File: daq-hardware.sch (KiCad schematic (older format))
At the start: 26 parts

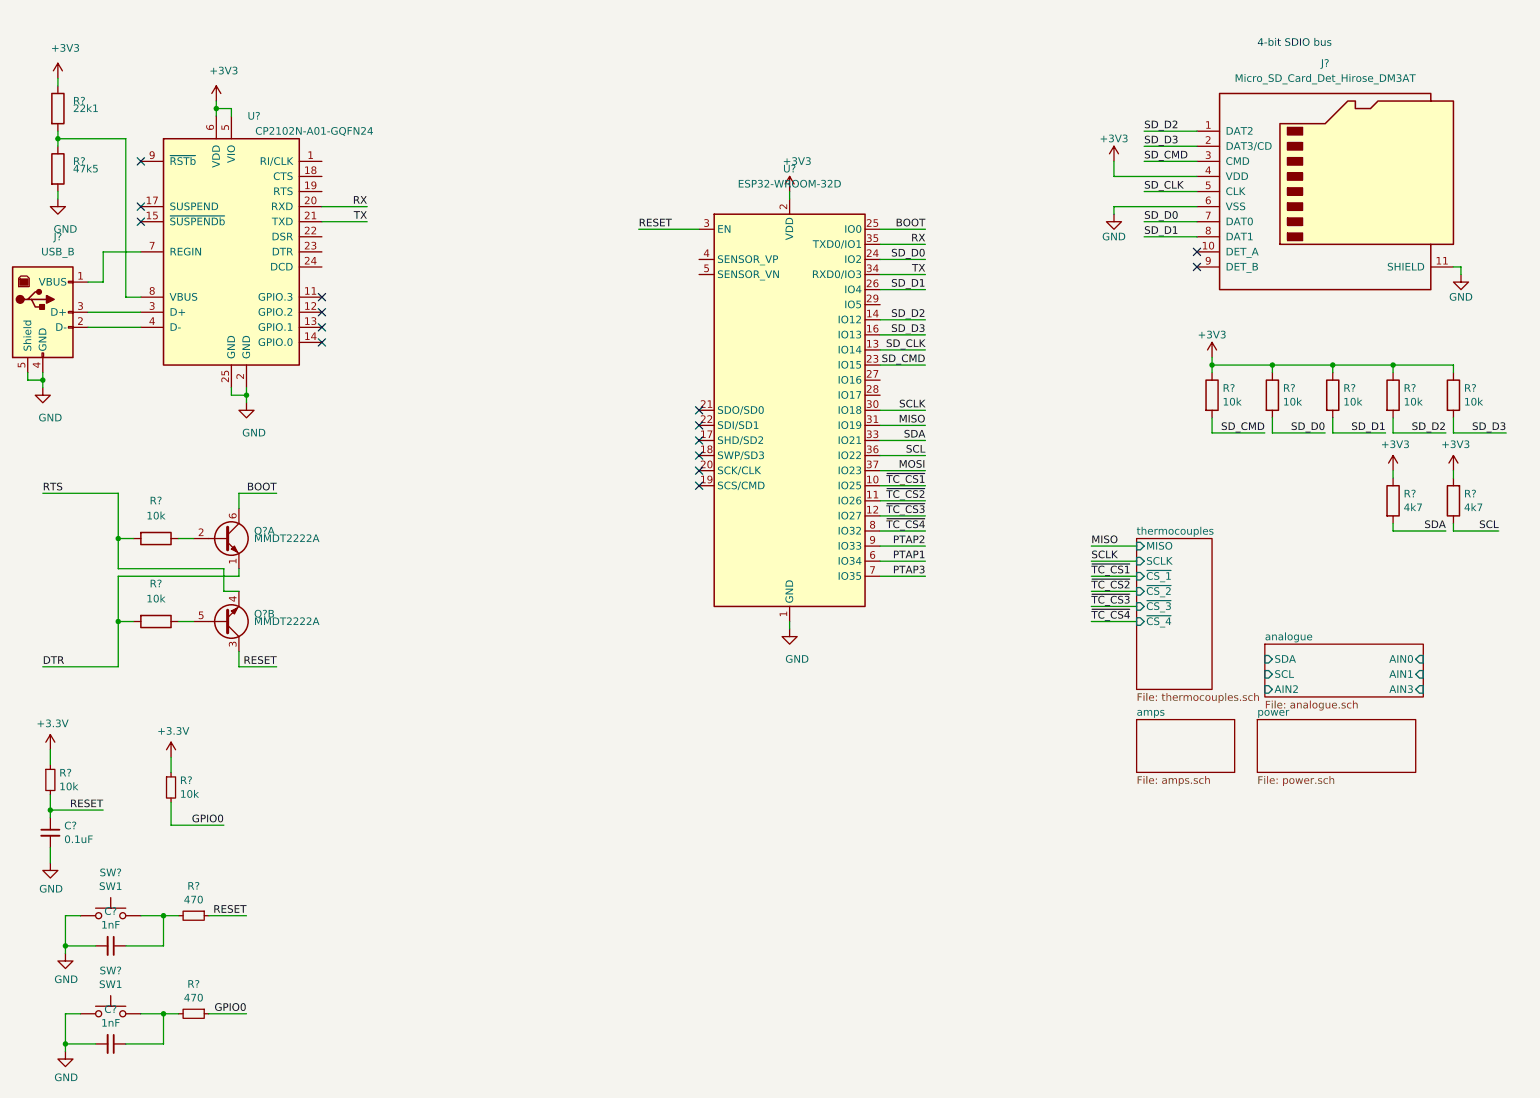
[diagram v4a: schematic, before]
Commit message: Added indicator LEDs
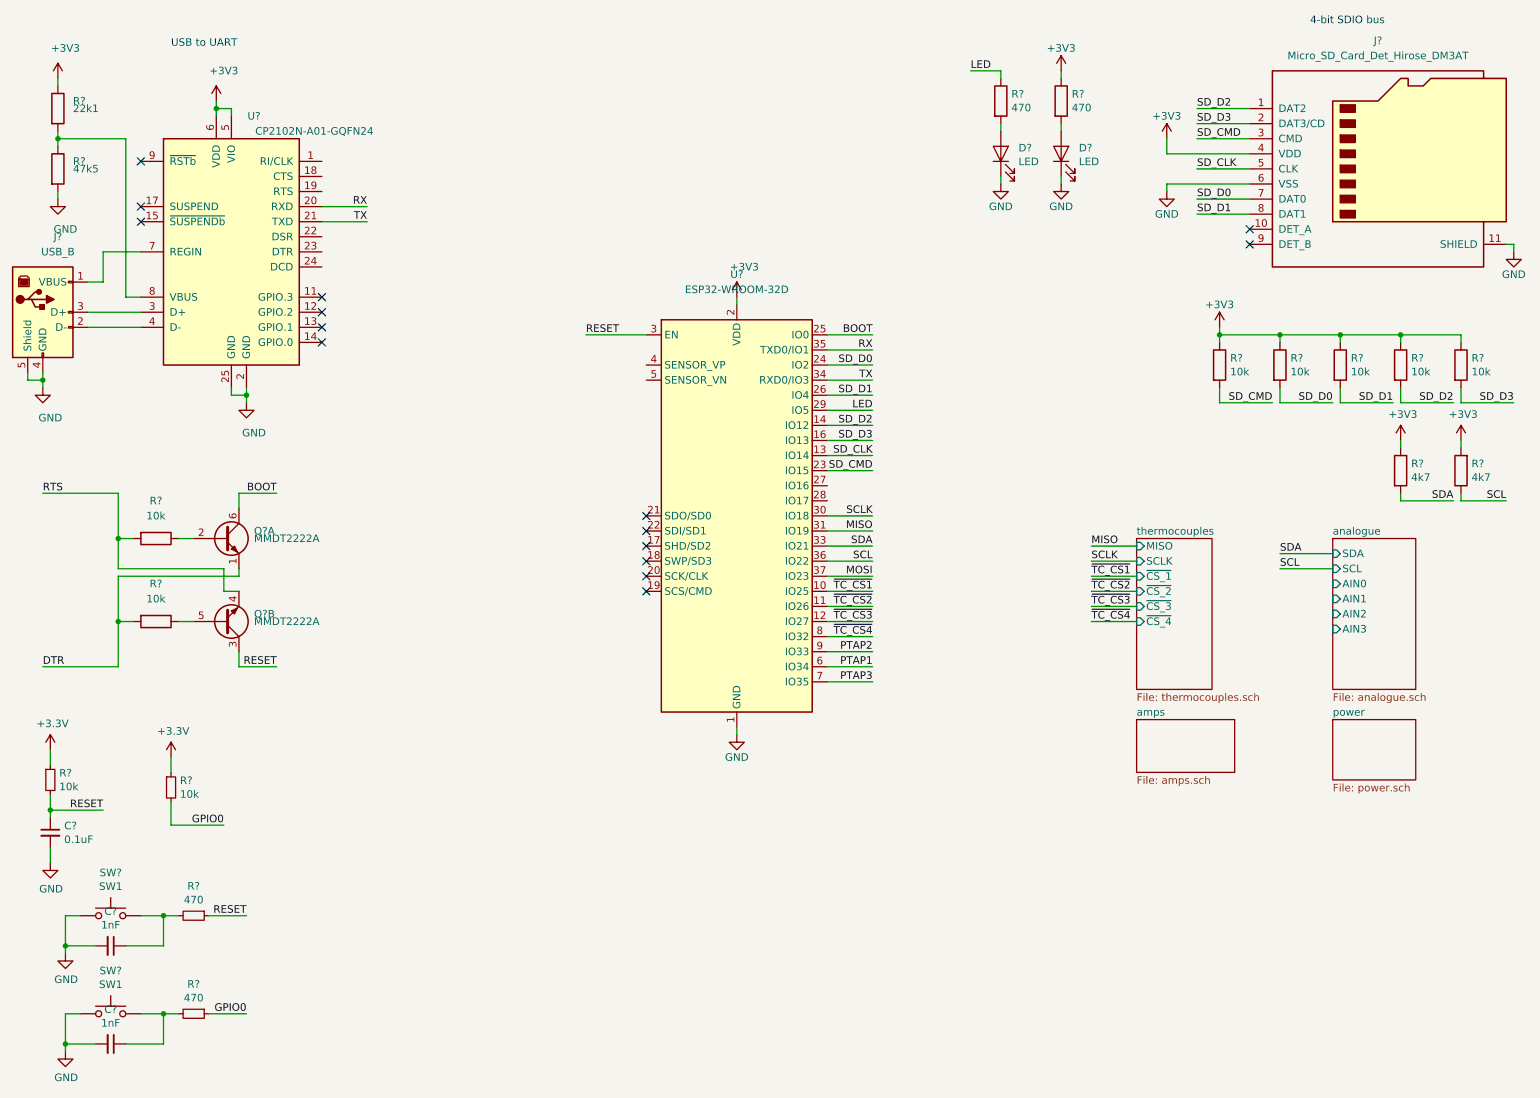
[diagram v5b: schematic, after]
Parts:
- added D? (x2): LED, symbol Device:LED
- added R? (x2): 470, symbol Device:R
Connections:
- net +3V3: now also R?.1
- net GND: now also D?.1 (K), D?.1 (K)
- net LED: now reaches U?.29 (IO5)
- net LED: now also R?.1
- new net: D?.2 (A), R?.2 (x2)
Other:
- note added: "USB to UART"
- moved on the sheet: J?, R?, U?

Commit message: Pyros
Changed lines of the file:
@@
 $Descr A4 11693 8268
 encoding utf-8
-Sheet 1 5
+Sheet 1 6
 Title ""
 Date ""
@@
 Text Label 6850 3200 2    50   ~ 0
 LED
+$Sheet
+S 7350 5250 650  350
+U 5DB4FA2A
+F0 "pyro" 50
+F1 "pyro.sch" 50
+F2 "Fire" I L 7350 5350 50
+$EndSheet
 $EndSCHEMATC

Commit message: changed the hierarchical pins of the analogue
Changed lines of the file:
@@
 Text Label 6850 2700 2    50   ~ 0
 BOOT
-$Sheet
-S 9900 4050 550  1000
-U 5DA926B9
-F0 "analogue" 50
-F1 "analogue.sch" 50
-F2 "SDA" I L 9900 4150 50
-F3 "SCL" I L 9900 4250 50
-F4 "AIN0" I L 9900 4350 50
-F5 "AIN1" I L 9900 4450 50
-F6 "AIN3" I L 9900 4650 50
-F7 "AIN2" I L 9900 4550 50
-$EndSheet
 NoConn ~ 9350 2100
 NoConn ~ 9350 2000
@@
 NoConn ~ 5350 4300
 NoConn ~ 5350 4400
-Wire Wire Line
-	9900 4150 9550 4150
-Text Label 9550 4150 0    50   ~ 0
-SDA
-Wire Wire Line
-	9900 4250 9550 4250
-Text Label 9550 4250 0    50   ~ 0
-SCL
 Text Notes 2200 800  0    50   ~ 0
 USB to UART
@@
 F2 "Fire" I L 7350 5350 50
 $EndSheet
+$Sheet
+S 9900 4050 550  1000
+U 5DA926B9
+F0 "analogue" 50
+F1 "analogue.sch" 50
+F2 "MOSI" I L 9900 4150 50
+F3 "MISO" O L 9900 4250 50
+F4 "SCLK" I L 9900 4350 50
+F5 "~CS" I L 9900 4450 50
+F6 "~DRDY" O L 9900 4550 50
+F7 "CLKIN" I L 9900 4650 50
+$EndSheet
 $EndSCHEMATC

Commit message: Not sure if this is gonna overwrite stuff but I try to push this anyway
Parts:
- gave numbers to parts that had none: 29
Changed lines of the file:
@@
 	5950 5350 5950 5300
 $Comp
-L Connector:USB_B J?
+L Connector:USB_B J1
 U 1 1 5DA63605
 P 1350 2550
-F 0 "J?" H 1450 3050 50  0000 C CNN
+F 0 "J1" H 1450 3050 50  0000 C CNN
 F 1 "USB_B" H 1450 2950 50  0000 C CNN
 F 2 "Connector_USB:USB_B_OST_USB-B1HSxx_Horizontal" H 1500 2500 50  0001 C CNN
@@
 $EndComp
 $Comp
-L Interface_USB:CP2102N-A01-GQFN24 U?
+L Interface_USB:CP2102N-A01-GQFN24 U1
 U 1 1 5DA64A7C
 P 2600 2150
-F 0 "U?" H 2750 3050 50  0000 C CNN
+F 0 "U1" H 2750 3050 50  0000 C CNN
 F 1 "CP2102N-A01-GQFN24" H 3150 2950 50  0000 C CNN
 F 2 "Package_DFN_QFN:QFN-24-1EP_4x4mm_P0.5mm_EP2.6x2.6mm" H 3050 1350 50  0001 L CNN
@@
 	2500 1200 2500 1250
 $Comp
-L RF_Module:ESP32-WROOM-32D U?
+L RF_Module:ESP32-WROOM-32D U2
 U 1 1 5DA60666
 P 5950 3900
-F 0 "U?" H 5950 5500 50  0000 C CNN
+F 0 "U2" H 5950 5500 50  0000 C CNN
 F 1 "ESP32-WROOM-32D" H 5950 5400 50  0000 C CNN
 F 2 "RF_Module:ESP32-WROOM-32" H 5950 2400 50  0001 C CNN
@@
 	1750 2150 2000 2150
 $Comp
-L Device:R R?
+L Device:R R2
 U 1 1 5DA6B300
 P 1450 1200
-F 0 "R?" H 1550 1250 50  0000 L CNN
+F 0 "R2" H 1550 1250 50  0000 L CNN
 F 1 "22k1" H 1550 1200 50  0000 L CNN
 F 2 "" V 1380 1200 50  0001 C CNN
@@
 $EndComp
 $Comp
-L Device:R R?
+L Device:R R3
 U 1 1 5DA6BB78
 P 1450 1600
-F 0 "R?" H 1550 1650 50  0000 L CNN
+F 0 "R3" H 1550 1650 50  0000 L CNN
 F 1 "47k5" H 1550 1600 50  0000 L CNN
 F 2 "" V 1380 1600 50  0001 C CNN
@@
 TX
 $Comp
-L Connector:Micro_SD_Card_Det_Hirose_DM3AT J?
+L Connector:Micro_SD_Card_Det_Hirose_DM3AT J2
 U 1 1 5DA72DEE
 P 10250 1600
-F 0 "J?" H 10200 2450 50  0000 C CNN
+F 0 "J2" H 10200 2450 50  0000 C CNN
 F 1 "Micro_SD_Card_Det_Hirose_DM3AT" H 10200 2350 50  0000 C CNN
 F 2 "Connector_Card:microSD_HC_Hirose_DM3AT-SF-PEJM5" H 12300 2300 50  0001 C CNN
@@
 	8800 1700 9350 1700
 $Comp
-L Transistor_BJT:MMDT2222A Q?
+L Transistor_BJT:MMDT2222A Q1
 U 1 1 5DA77BBC
 P 2550 4050
-F 0 "Q?" H 2750 4100 50  0000 L CNN
+F 0 "Q1" H 2750 4100 50  0000 L CNN
 F 1 "MMDT2222A" H 2750 4050 50  0000 L CNN
 F 2 "Package_TO_SOT_SMD:SOT-363_SC-70-6" H 2750 4150 50  0001 C CNN
@@
 $EndComp
 $Comp
-L Transistor_BJT:MMDT2222A Q?
+L Transistor_BJT:MMDT2222A Q1
 U 2 1 5DA7899D
 P 2550 4600
-F 0 "Q?" H 2750 4550 50  0000 L CNN
+F 0 "Q1" H 2750 4550 50  0000 L CNN
 F 1 "MMDT2222A" H 2750 4600 50  0000 L CNN
 F 2 "Package_TO_SOT_SMD:SOT-363_SC-70-6" H 2750 4700 50  0001 C CNN
@@
 $EndComp
 $Comp
-L Device:R R?
+L Device:R R4
 U 1 1 5DA7B0F5
 P 2100 4050
-F 0 "R?" V 1850 4050 50  0000 C CNN
+F 0 "R4" V 1850 4050 50  0000 C CNN
 F 1 "10k" V 1950 4050 50  0000 C CNN
 F 2 "Resistor_SMD:R_0603_1608Metric" V 2030 4050 50  0001 C CNN
@@
 $EndComp
 $Comp
-L Device:R R?
+L Device:R R5
 U 1 1 5DA7B96F
 P 2100 4600
-F 0 "R?" V 1850 4600 50  0000 C CNN
+F 0 "R5" V 1850 4600 50  0000 C CNN
 F 1 "10k" V 1950 4600 50  0000 C CNN
 F 2 "Resistor_SMD:R_0603_1608Metric" V 2030 4600 50  0001 C CNN
@@
 MOSI
 $Comp
-L Device:R_Small R?
+L Device:R_Small R1
 U 1 1 5DBE20E6
 P 1400 5650
-F 0 "R?" H 1459 5696 50  0000 L CNN
+F 0 "R1" H 1459 5696 50  0000 L CNN
 F 1 "10k" H 1459 5605 50  0000 L CNN
 F 2 "" H 1400 5650 50  0001 C CNN
@@
 $EndComp
 $Comp
-L Device:C_Small C?
+L Device:C_Small C1
 U 1 1 5DBE24AB
 P 1400 6000
-F 0 "C?" H 1492 6046 50  0000 L CNN
+F 0 "C1" H 1492 6046 50  0000 L CNN
 F 1 "0.1uF" H 1492 5955 50  0000 L CNN
 F 2 "" H 1400 6000 50  0001 C CNN
@@
 $EndComp
 $Comp
-L Device:R_Small R?
+L Device:R_Small R6
 U 1 1 5DBEB1F6
 P 2200 5700
-F 0 "R?" H 2259 5746 50  0000 L CNN
+F 0 "R6" H 2259 5746 50  0000 L CNN
 F 1 "10k" H 2259 5655 50  0000 L CNN
 F 2 "" H 2200 5700 50  0001 C CNN
@@
 GPIO0
 $Comp
-L Switch:SW_Push SW?
+L Switch:SW_Push SW1
 U 1 1 5DBEEFD5
 P 1800 6550
-F 0 "SW?" H 1800 6835 50  0000 C CNN
+F 0 "SW1" H 1800 6835 50  0000 C CNN
 F 1 "SW1" H 1800 6744 50  0000 C CNN
 F 2 "" H 1800 6750 50  0001 C CNN
@@
 $EndComp
 $Comp
-L Device:C_Small C?
+L Device:C_Small C2
 U 1 1 5DBF1E6A
 P 1800 6750
-F 0 "C?" V 1571 6750 50  0000 C CNN
+F 0 "C2" V 1571 6750 50  0000 C CNN
 F 1 "1nF" V 1662 6750 50  0000 C CNN
 F 2 "" H 1800 6750 50  0001 C CNN
@@
 $EndComp
 $Comp
-L Device:R_Small R?
+L Device:R_Small R7
 U 1 1 5DBF243C
 P 2350 6550
-F 0 "R?" V 2154 6550 50  0000 C CNN
+F 0 "R7" V 2154 6550 50  0000 C CNN
 F 1 "470" V 2245 6550 50  0000 C CNN
 F 2 "" H 2350 6550 50  0001 C CNN
@@
 	2700 6550 2450 6550
 $Comp
-L Switch:SW_Push SW?
+L Switch:SW_Push SW2
 U 1 1 5DBFE9BD
 P 1800 7200
-F 0 "SW?" H 1800 7485 50  0000 C CNN
+F 0 "SW2" H 1800 7485 50  0000 C CNN
 F 1 "SW1" H 1800 7394 50  0000 C CNN
 F 2 "" H 1800 7400 50  0001 C CNN
@@
 $EndComp
 $Comp
-L Device:C_Small C?
+L Device:C_Small C3
 U 1 1 5DBFE9C9
 P 1800 7400
-F 0 "C?" V 1571 7400 50  0000 C CNN
+F 0 "C3" V 1571 7400 50  0000 C CNN
 F 1 "1nF" V 1662 7400 50  0000 C CNN
 F 2 "" H 1800 7400 50  0001 C CNN
@@
 $EndComp
 $Comp
-L Device:R_Small R?
+L Device:R_Small R8
 U 1 1 5DBFE9CF
 P 2350 7200
-F 0 "R?" V 2154 7200 50  0000 C CNN
+F 0 "R8" V 2154 7200 50  0000 C CNN
 F 1 "470" V 2245 7200 50  0000 C CNN
 F 2 "" H 2350 7200 50  0001 C CNN
@@
 P 10350 3600
 AR Path="/5DA926B9/5DB5090D" Ref="R?"  Part="1"
-AR Path="/5DB5090D" Ref="R?"  Part="1"
-F 0 "R?" H 10420 3646 50  0000 L CNN
+AR Path="/5DB5090D" Ref="R15"  Part="1"
+F 0 "R15" H 10420 3646 50  0000 L CNN
 F 1 "4k7" H 10420 3555 50  0000 L CNN
 F 2 "" V 10280 3600 50  0001 C CNN
@@
 P 10750 3600
 AR Path="/5DA926B9/5DB50914" Ref="R?"  Part="1"
-AR Path="/5DB50914" Ref="R?"  Part="1"
-F 0 "R?" H 10680 3554 50  0000 R CNN
+AR Path="/5DB50914" Ref="R17"  Part="1"
+F 0 "R17" H 10680 3554 50  0000 R CNN
 F 1 "4k7" H 10680 3645 50  0000 R CNN
 F 2 "" V 10680 3600 50  0001 C CNN
@@
 P 9550 2900
 AR Path="/5DA926B9/5DB6C807" Ref="R?"  Part="1"
-AR Path="/5DB6C807" Ref="R?"  Part="1"
-F 0 "R?" H 9620 2946 50  0000 L CNN
+AR Path="/5DB6C807" Ref="R12"  Part="1"
+F 0 "R12" H 9620 2946 50  0000 L CNN
 F 1 "10k" H 9620 2855 50  0000 L CNN
 F 2 "" V 9480 2900 50  0001 C CNN
@@
 P 10750 2900
 AR Path="/5DA926B9/5DB6D7EC" Ref="R?"  Part="1"
-AR Path="/5DB6D7EC" Ref="R?"  Part="1"
-F 0 "R?" H 10820 2946 50  0000 L CNN
+AR Path="/5DB6D7EC" Ref="R16"  Part="1"
+F 0 "R16" H 10820 2946 50  0000 L CNN
 F 1 "10k" H 10820 2855 50  0000 L CNN
 F 2 "" V 10680 2900 50  0001 C CNN
@@
 P 10350 2900
 AR Path="/5DA926B9/5DB6D360" Ref="R?"  Part="1"
-AR Path="/5DB6D360" Ref="R?"  Part="1"
-F 0 "R?" H 10420 2946 50  0000 L CNN
+AR Path="/5DB6D360" Ref="R14"  Part="1"
+F 0 "R14" H 10420 2946 50  0000 L CNN
 F 1 "10k" H 10420 2855 50  0000 L CNN
 F 2 "" V 10280 2900 50  0001 C CNN
@@
 P 9950 2900
 AR Path="/5DA926B9/5DB6CAE9" Ref="R?"  Part="1"
-AR Path="/5DB6CAE9" Ref="R?"  Part="1"
-F 0 "R?" H 10020 2946 50  0000 L CNN
+AR Path="/5DB6CAE9" Ref="R13"  Part="1"
+F 0 "R13" H 10020 2946 50  0000 L CNN
 F 1 "10k" H 10020 2855 50  0000 L CNN
 F 2 "" V 9880 2900 50  0001 C CNN
@@
 P 9150 2900
 AR Path="/5DA926B9/5DB6C1D1" Ref="R?"  Part="1"
-AR Path="/5DB6C1D1" Ref="R?"  Part="1"
-F 0 "R?" H 9220 2946 50  0000 L CNN
+AR Path="/5DB6C1D1" Ref="R11"  Part="1"
+F 0 "R11" H 9220 2946 50  0000 L CNN
 F 1 "10k" H 9220 2855 50  0000 L CNN
 F 2 "" V 9080 2900 50  0001 C CNN
@@
 $EndComp
 $Comp
-L Device:LED D?
+L Device:LED D2
 U 1 1 5DCBE0CD
 P 8100 1500
-F 0 "D?" V 8139 1383 50  0000 R CNN
+F 0 "D2" V 8139 1383 50  0000 R CNN
 F 1 "LED" V 8048 1383 50  0000 R CNN
 F 2 "" H 8100 1500 50  0001 C CNN
@@
 $EndComp
 $Comp
-L power:GND #PWR?
+L power:GND #PWR0119
 U 1 1 5DCC16C2
 P 8100 1700
-F 0 "#PWR?" H 8100 1450 50  0001 C CNN
+F 0 "#PWR0119" H 8100 1450 50  0001 C CNN
 F 1 "GND" H 8100 1550 50  0000 C CNN
 F 2 "" H 8100 1700 50  0001 C CNN
@@
 	8100 1700 8100 1650
 $Comp
-L power:+3V3 #PWR?
+L power:+3V3 #PWR0120
 U 1 1 5DCC78DF
 P 8100 950
-F 0 "#PWR?" H 8100 800 50  0001 C CNN
+F 0 "#PWR0120" H 8100 800 50  0001 C CNN
 F 1 "+3V3" H 8100 1100 50  0000 C CNN
 F 2 "" H 8100 950 50  0001 C CNN
@@
 P 8100 1150
 AR Path="/5DA926B9/5DCCDB3E" Ref="R?"  Part="1"
-AR Path="/5DCCDB3E" Ref="R?"  Part="1"
-F 0 "R?" H 8170 1196 50  0000 L CNN
+AR Path="/5DCCDB3E" Ref="R10"  Part="1"
+F 0 "R10" H 8170 1196 50  0000 L CNN
 F 1 "470" H 8170 1105 50  0000 L CNN
 F 2 "" V 8030 1150 50  0001 C CNN
@@
 	8100 1000 8100 950
 $Comp
-L Device:LED D?
+L Device:LED D1
 U 1 1 5DCDED54
 P 7700 1500
-F 0 "D?" V 7739 1383 50  0000 R CNN
+F 0 "D1" V 7739 1383 50  0000 R CNN
 F 1 "LED" V 7648 1383 50  0000 R CNN
 F 2 "" H 7700 1500 50  0001 C CNN
@@
 $EndComp
 $Comp
-L power:GND #PWR?
+L power:GND #PWR0121
 U 1 1 5DCDED5E
 P 7700 1700
-F 0 "#PWR?" H 7700 1450 50  0001 C CNN
+F 0 "#PWR0121" H 7700 1450 50  0001 C CNN
 F 1 "GND" H 7700 1550 50  0000 C CNN
 F 2 "" H 7700 1700 50  0001 C CNN
@@
 P 7700 1150
 AR Path="/5DA926B9/5DCDED73" Ref="R?"  Part="1"
-AR Path="/5DCDED73" Ref="R?"  Part="1"
-F 0 "R?" H 7770 1196 50  0000 L CNN
+AR Path="/5DCDED73" Ref="R9"  Part="1"
+F 0 "R9" H 7770 1196 50  0000 L CNN
 F 1 "470" H 7770 1105 50  0000 L CNN
 F 2 "" V 7630 1150 50  0001 C CNN
